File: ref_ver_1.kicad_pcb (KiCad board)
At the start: 2 copper layers, 129 x 90 mm, 21 parts, among them J1 Conn_01x03_Pin, J2 Conn_01x03_Pin, J3 Conn_01x03_Pin, J4 Conn_01x04_Pin, U1 LM399, U2 LTC2057IS8-TRPBF, U3 SHT4x

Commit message: updated to new revision
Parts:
- added C7: 100n, Capacitor_SMD:C_0603_1608Metric_Pad1.08x0.95mm_HandSolder, F.Cu at (146.7, 98.4)
- added C8: 10n, Capacitor_SMD:C_0603_1608Metric_Pad1.08x0.95mm_HandSolder, F.Cu at (157.5, 98.2)
- moved R5 35.0 mm to (147.0, 102.9), turned to 180 degrees
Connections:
- R1 pad 3: /OUT -> Net-(J2-Pin_3)
- R3 pad 2: /OUT -> Net-(J2-Pin_3)
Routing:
- net GND: track 482.3 -> 407.4 mm
- net Net-(J2-Pin_3): track 17.7 -> 83.5 mm, vias 0 -> 4
- net /OUT: track 60.7 -> 4.85 mm, vias 3 -> 0
- net VCC: track 114.1 -> 121.2 mm
- net /IN-: track 19.5 -> 25.4 mm
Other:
- board text added: "LM399 Reference by Simon Bauch DB4UCH V0.1.1 2025"
- board text removed: "LM399 Reference by Simon Bauch DB4UCH V0.1 2025"

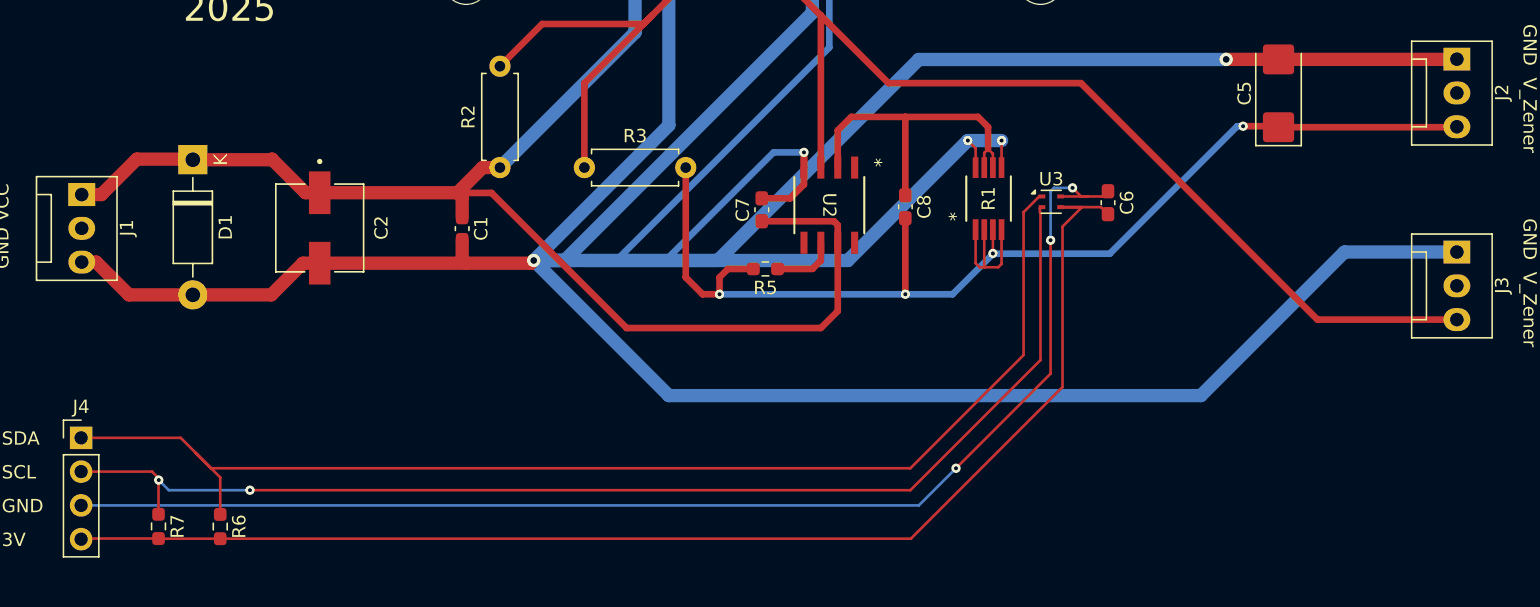
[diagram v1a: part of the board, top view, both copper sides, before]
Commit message: Small changes to the PCB before production
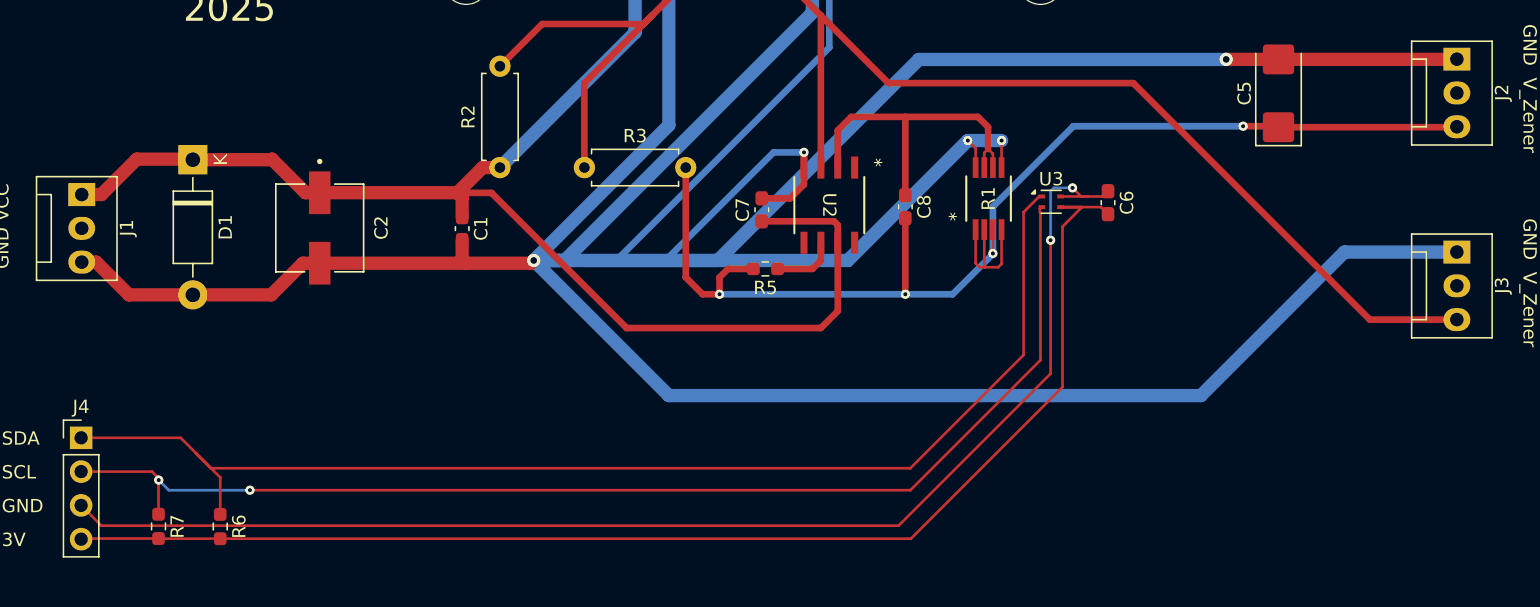
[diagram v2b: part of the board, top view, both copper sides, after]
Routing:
- net Net-(J2-Pin_3): track 83.5 -> 85.6 mm
- net GND1: track 97.6 -> 98.9 mm, vias 3 -> 2
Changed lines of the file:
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@@
 	)
 	(segment
-		(start 164.084 101.727)
+		(start 182.88 92.14)
+		(end 170.115 92.14)
+		(width 0.5)
+		(layer "B.Cu")
+		(net 4)
+	)
+	(segment
+		(start 164.065001 98.189999)
 		(end 164.065001 101.708001)
-		(width 0.5)
-		(layer "B.Cu")
-		(net 4)
-	)
-	(segment
-		(start 182.434 92.14)
-		(end 172.847 101.727)
 		(width 0.5)
 		(layer "B.Cu")
@@
 	)
 	(segment
+		(start 170.115 92.14)
+		(end 164.065001 98.189999)
+		(width 0.5)
+		(layer "B.Cu")
+		(net 4)
+	)
+	(segment
 		(start 143.51 104.775)
 		(end 161.036 104.775)
@@
 	)
 	(segment
-		(start 182.88 92.14)
-		(end 182.434 92.14)
-		(width 0.5)
-		(layer "B.Cu")
-		(net 4)
-	)
-	(segment
-		(start 172.847 101.727)
-		(end 164.084 101.727)
-		(width 0.5)
-		(layer "B.Cu")
-		(net 4)
-	)
-	(segment
 		(start 164.714999 99.9109)
 		(end 164.714999 102.493001)
@@
 	)
 	(segment
-		(start 161.29 117.856)
+		(start 156.972 122.174)
+		(end 97.034 122.174)
+		(width 0.2)
+		(layer "F.Cu")
+		(net 12)
+	)
+	(segment
+		(start 168.402 110.744)
+		(end 156.972 122.174)
+		(width 0.2)
+		(layer "F.Cu")
+		(net 12)
+	)
+	(segment
+		(start 168.402 100.711)
 		(end 168.402 110.744)
-		(width 0.2)
-		(layer "F.Cu")
-		(net 12)
-	)
-	(segment
-		(start 168.402 110.744)
-		(end 168.402 100.711)
 		(width 0.2)
 		(layer "F.Cu")
@@
 	)
 	(segment
+		(start 97.034 122.174)
+		(end 95.51 120.65)
+		(width 0.2)
+		(layer "F.Cu")
+		(net 12)
+	)
+	(segment
 		(start 169.15 97.423)
 		(end 171.196 97.423)
 		(width 0.2)
 		(layer "F.Cu")
-		(net 12)
-	)
-	(via
-		(at 161.29 117.856)
-		(size 0.7)
-		(drill 0.3)
-		(layers "F.Cu" "B.Cu")
 		(net 12)
 	)
@@
 	)
 	(segment
-		(start 158.496 120.65)
-		(end 161.29 117.856)
-		(width 0.2)
-		(layer "B.Cu")
-		(net 12)
-	)
-	(segment
 		(start 168.402 100.711)
 		(end 168.402 97.028)
-		(width 0.2)
-		(layer "B.Cu")
-		(net 12)
-	)
-	(segment
-		(start 95.51 120.65)
-		(end 158.496 120.65)
 		(width 0.2)
 		(layer "B.Cu")
@@
 	)
 	(segment
-		(start 188.468 106.68)
-		(end 198.95 106.68)
-		(width 0.5)
-		(layer "F.Cu")
-		(net 18)
-	)
-	(segment
 		(start 147.32 73.73)
 		(end 147.32 80.01)
@@
 	(segment
 		(start 156.21 88.9)
-		(end 170.688 88.9)
+		(end 174.625 88.9)
 		(width 0.5)
 		(layer "F.Cu")
@@
 	)
 	(segment
-		(start 151.13 83.82)
-		(end 156.21 88.9)
-		(width 0.5)
-		(layer "F.Cu")
-		(net 18)
-	)
-	(segment
 		(start 147.32 80.01)
 		(end 151.13 83.82)
+		(width 0.5)
+		(layer "F.Cu")
+		(net 18)
+	)
+	(segment
+		(start 192.405 106.68)
+		(end 198.95 106.68)
 		(width 0.5)
 		(layer "F.Cu")
@@
 	)
 	(segment
-		(start 170.688 88.9)
-		(end 188.468 106.68)
-		(width 0.5)
-		(layer "F.Cu")
+		(start 174.625 88.9)
+		(end 192.405 106.68)
+		(width 0.5)
+		(layer "F.Cu")
+		(net 18)
+	)
+	(segment
+		(start 151.13 83.82)
+		(end 156.21 88.9)
+		(width 0.5)
+		(layer "F.Cu")
